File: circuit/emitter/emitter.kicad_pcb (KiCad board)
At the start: 2 copper layers, 34.5 x 23 mm, 8 parts, among them J1 Battery, J2 Cluster Node, U1 XIAO-nRF52840-SMD

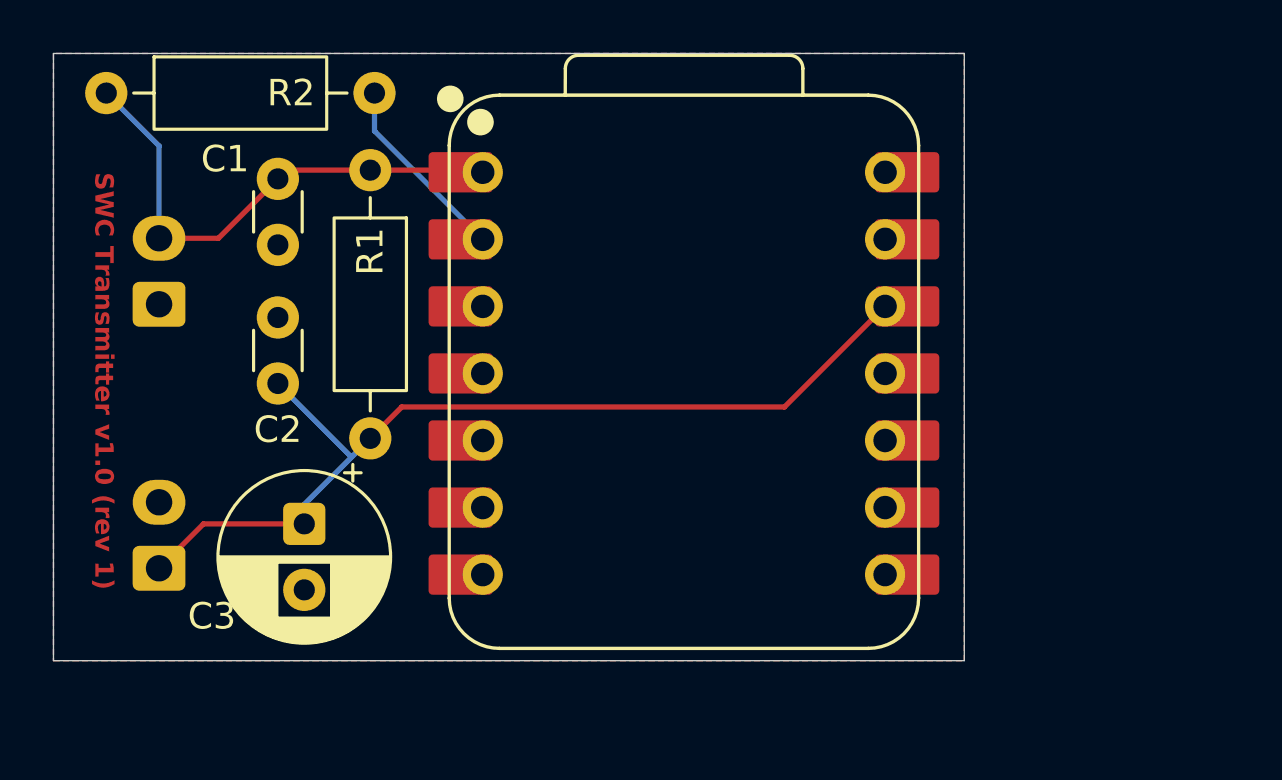
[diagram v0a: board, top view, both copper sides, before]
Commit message: refactor: add labels to circuits
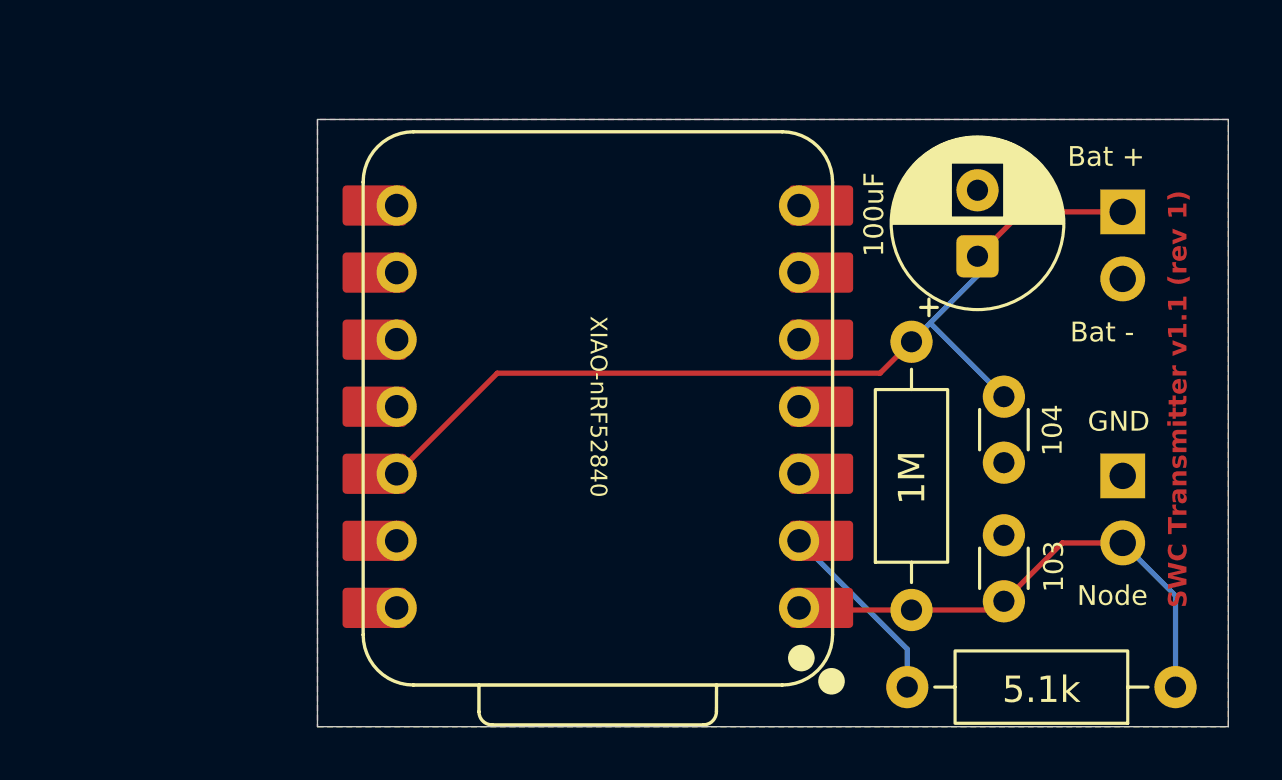
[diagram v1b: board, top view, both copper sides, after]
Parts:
- removed U1: XIAO-nRF52840-SMD, 01 Custom:XIAO-nRF52840-DIP
- added XIAO-nRF52840: XIAO-nRF52840, 01 Custom:XIAO-nRF52840-DIP, F.Cu at (128.6, 123.9)
- Bat +: renamed from J1; footprint Connector_JST:JST_XH_B2B-XH-A_1x02_P2.50mm_Vertical -> Connector_PinHeader_2.54mm:PinHeader_1x02_P2.54mm_Vertical
- GND: renamed from J2; footprint Connector_JST:JST_XH_B2B-XH-A_1x02_P2.50mm_Vertical -> Connector_PinHeader_2.54mm:PinHeader_1x02_P2.54mm_Vertical
- moved 5.1k 46.3 mm to (150.5, 134.5), turned to 180 degrees
- moved Bat + 38.9 mm to (148.5, 116.5), turned to 180 degrees
- moved GND 37.1 mm to (148.5, 126.5), turned to 180 degrees
- moved 103 29.6 mm to (144.0, 128.8), turned to -90 degrees
- moved 104 28.0 mm to (144.0, 126.0), turned to 90 degrees
- moved 100uF 27.4 mm to (143.0, 118.2), turned to 90 degrees
- moved 1M 26.4 mm to (140.5, 131.6), turned to 90 degrees
- renumbered C3 to 100uF, C1 to 103, C2 to 104, R1 to 1M, R2 to 5.1k
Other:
- board text added: "Bat -"
- board text added: "Copyright (c) Abhijith Vijayan"
- board text added: "Node"
- board text added: "SWC Transmitter v1.1 (rev 1)"
- board text removed: "SWC Transmitter v1.0 (rev 1)"
